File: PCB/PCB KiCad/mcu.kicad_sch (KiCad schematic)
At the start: 3 parts, among them J2 Qwiic

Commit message: Minor schematic cleanup!
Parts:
- added A1: Arduino_UNO_R3, Module:Arduino_UNO_R3, symbol MCU_Module:Arduino_UNO_R3
- added D2: LED BLUE, LED_SMD:LED_0805_2012Metric_Pad1.15x1.40mm_HandSolder, symbol Device:LED
- added D3: LED RED, LED_SMD:LED_0805_2012Metric_Pad1.15x1.40mm_HandSolder, symbol Device:LED
- added J2: Conn_01x08, Connector_PinHeader_2.54mm:PinHeader_1x08_P2.54mm_Vertical, symbol Connector_Generic:Conn_01x08
- added R10, R9: 10k, Resistor_SMD:R_0805_2012Metric_Pad1.20x1.40mm_HandSolder, symbol Device:R
- added R12, R13: 4.7k, Resistor_SMD:R_0805_2012Metric_Pad1.20x1.40mm_HandSolder, symbol Device:R
- added R7, R8: 100, Resistor_SMD:R_0805_2012Metric_Pad1.20x1.40mm_HandSolder, symbol Device:R
- added SW1: MCU_RESET, Button_Switch_THT:SW_PUSH_6mm, symbol Switch:SW_Push
- added SW2: TRIGGER, Button_Switch_THT:SW_PUSH_6mm, symbol Switch:SW_Push
- renumbered D2 to D12, J2 to J3, R7 to R11
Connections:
- net +3V3 is gone; now on net 3v3unf: R11.1
- net 3v3unf: now also J2.2 (Pin_2)
- net GND: now also A1.29 (GND), A1.6 (GND), A1.7 (GND), D2.1 (K), D3.1 (K), J2.1 (Pin_1), SW1.1, SW2.1
- net SCL: now also A1.32 (SCL/A5), J2.4 (Pin_4), R13.2
- net SDA: now also A1.31 (SDA/A4), J2.3 (Pin_3), R12.2
- new net: D3.2 (A), R8.2
- new net: D2.2 (A), R7.2
- new net +3.3V: R12.1, R13.1
- new net 5v_RAW: A1.5 (+5V), J2.8 (Pin_8), R10.1, R8.1, R9.1
- new net DRDY_INT: A1.20 (D5), J2.6 (Pin_6)
- new net LED_BLUE: A1.19 (D4), R7.1
- new net LED_RESET: A1.17 (D2), J2.5 (Pin_5)
- new net MCU_RESET: A1.3 (~{RESET}), R9.2, SW1.2
- new net TRIGGER: A1.18 (D3), J2.7 (Pin_7), R10.2, SW2.2
- no-connect marks 0 -> 20
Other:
- note added: "Buttons"
- note added: "LEDs"
- note added: "hace default i2c output"
- note added: "potential problem logic is at 5v potential solution logic level shifter"
- moved on the sheet: D12, J3, R11

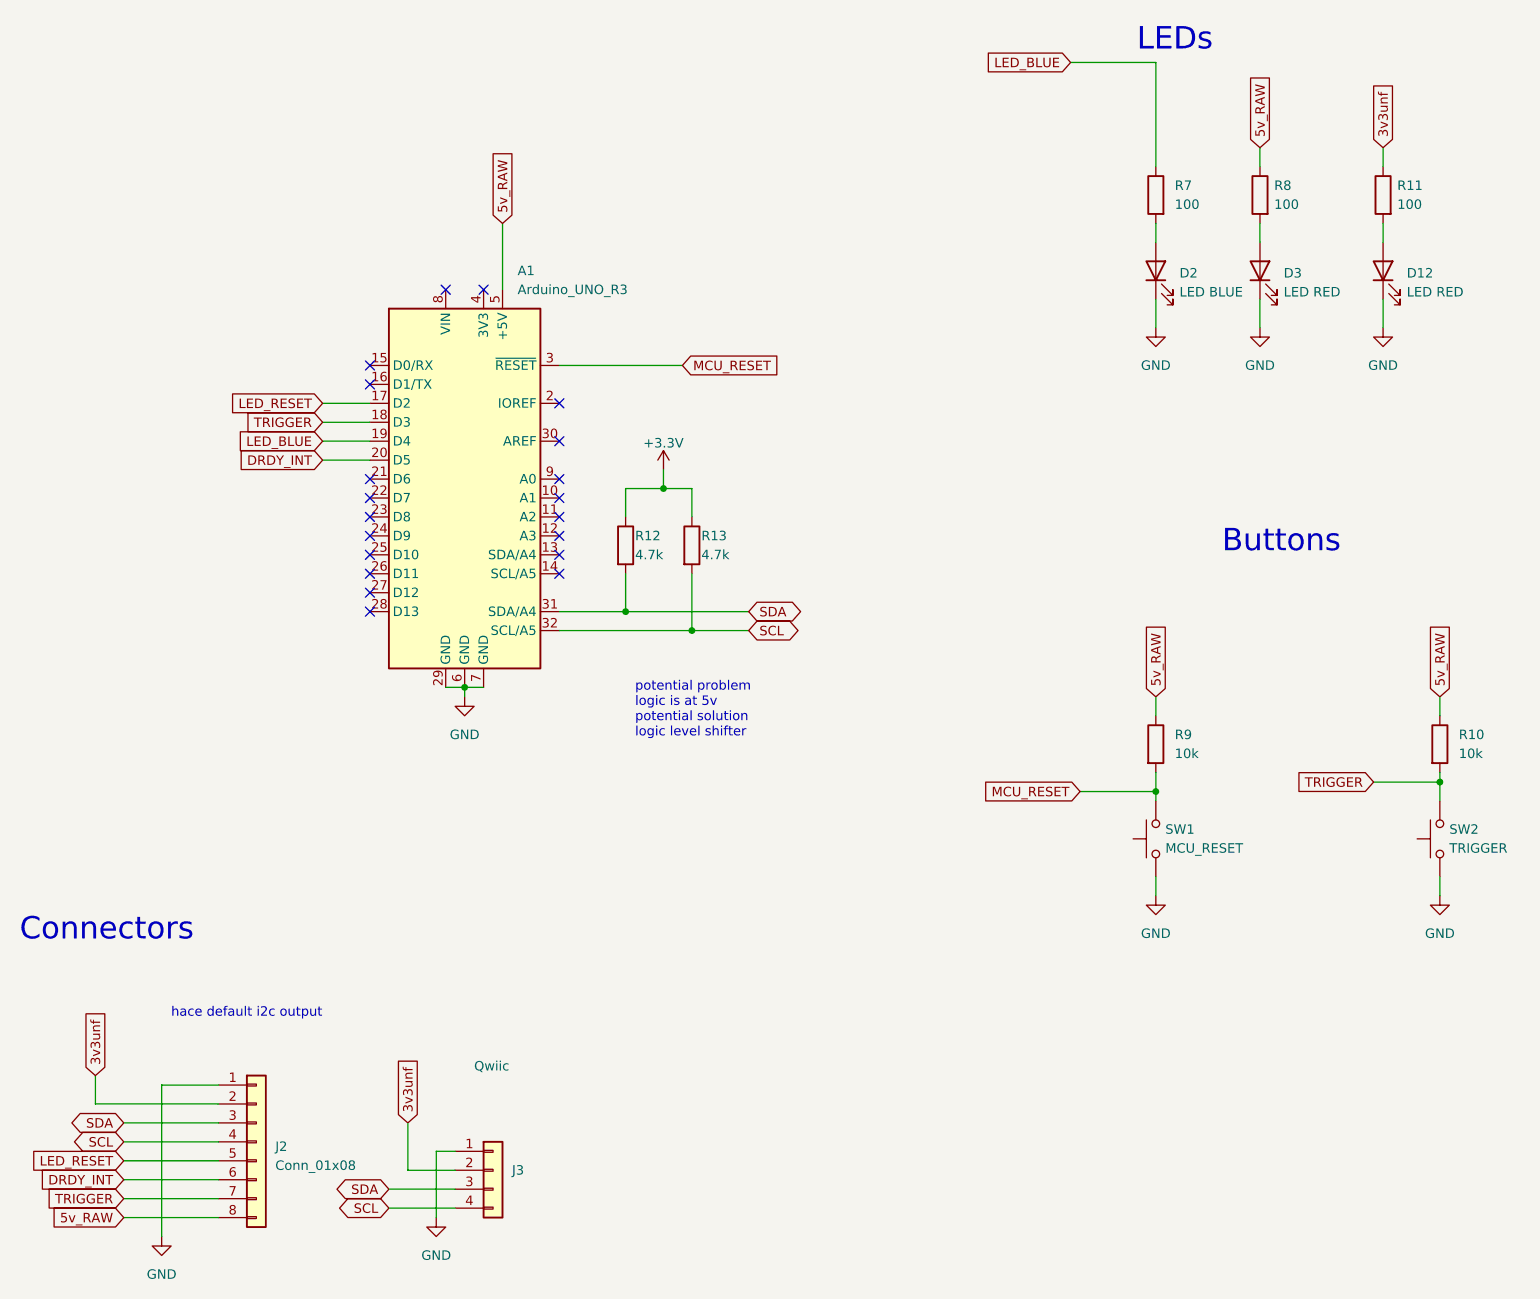
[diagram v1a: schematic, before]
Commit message: Giant schematic cleanup to make more sense of the sensor circuit and just clean everything up a bit.
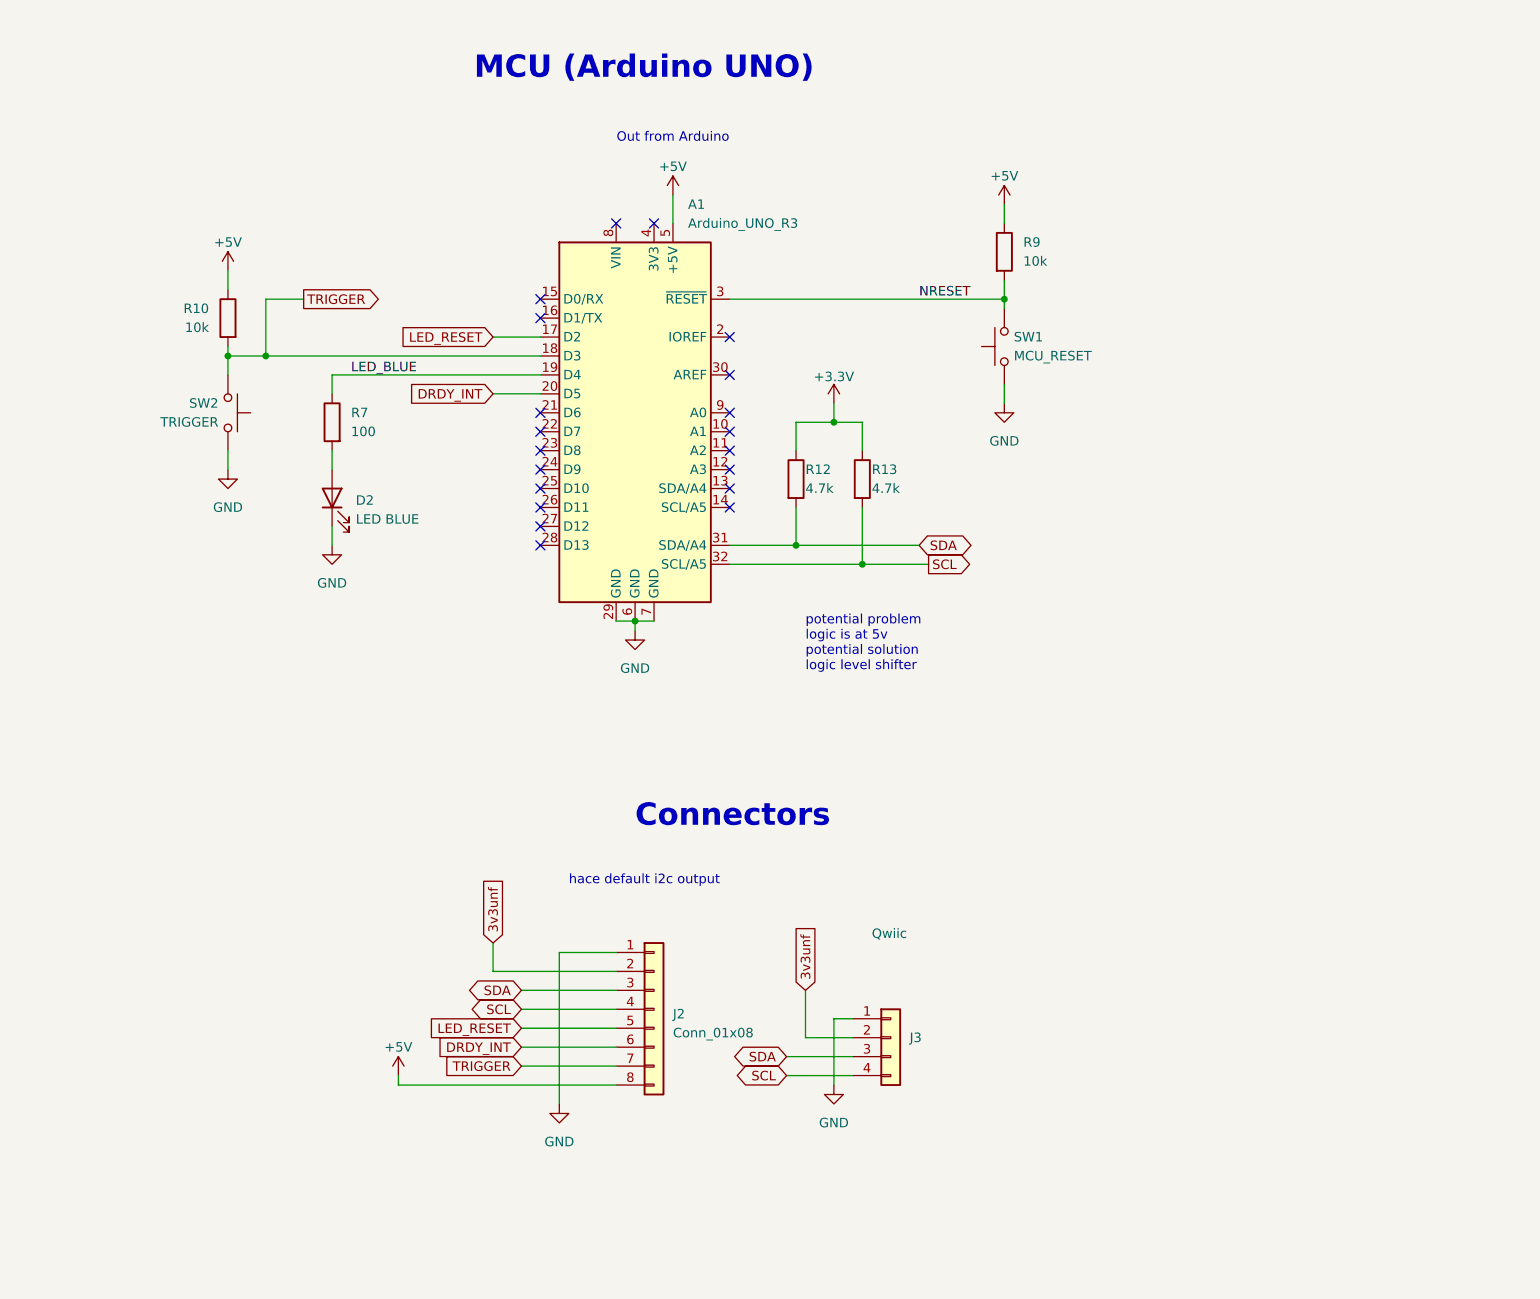
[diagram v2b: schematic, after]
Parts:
- removed D12, D3: LED RED, LED_SMD:LED_0805_2012Metric_Pad1.15x1.40mm_HandSolder, symbol Device:LED
- removed R11, R8: 100, Resistor_SMD:R_0805_2012Metric_Pad1.20x1.40mm_HandSolder, symbol Device:R
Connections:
- net 5v_RAW renamed +5V
- net MCU_RESET renamed NRESET
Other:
- note added: "MCU (Arduino UNO)"
- note added: "Out from Arduino"
- note removed: "Buttons"
- note removed: "LEDs"
- moved on the sheet: A1, D2, J2, J3, R10, R12, R13, R7, R9, SW1, SW2
